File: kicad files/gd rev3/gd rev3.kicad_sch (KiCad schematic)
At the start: 0 parts

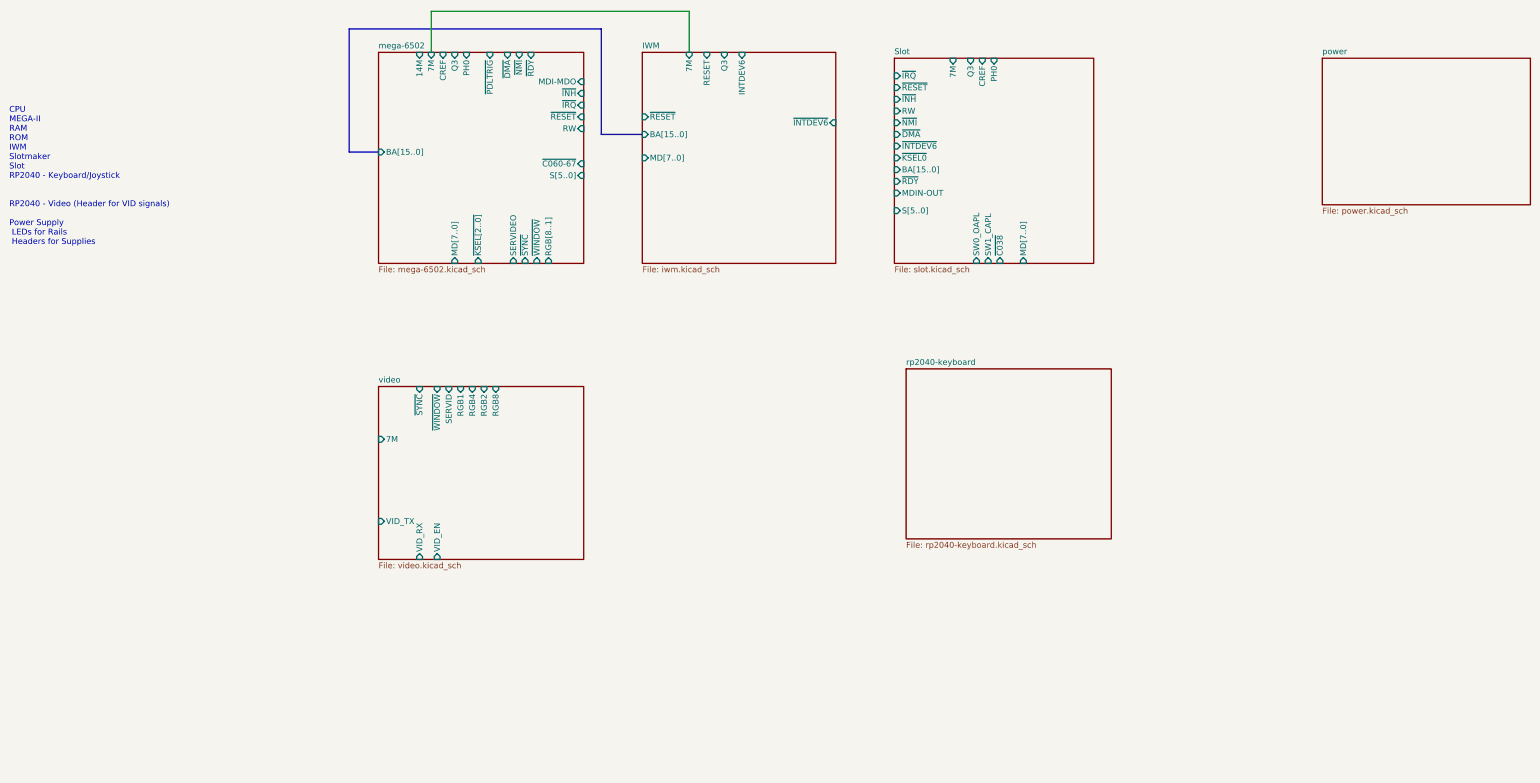
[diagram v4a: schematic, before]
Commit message: KBD Video and Power sheet labels, initial create
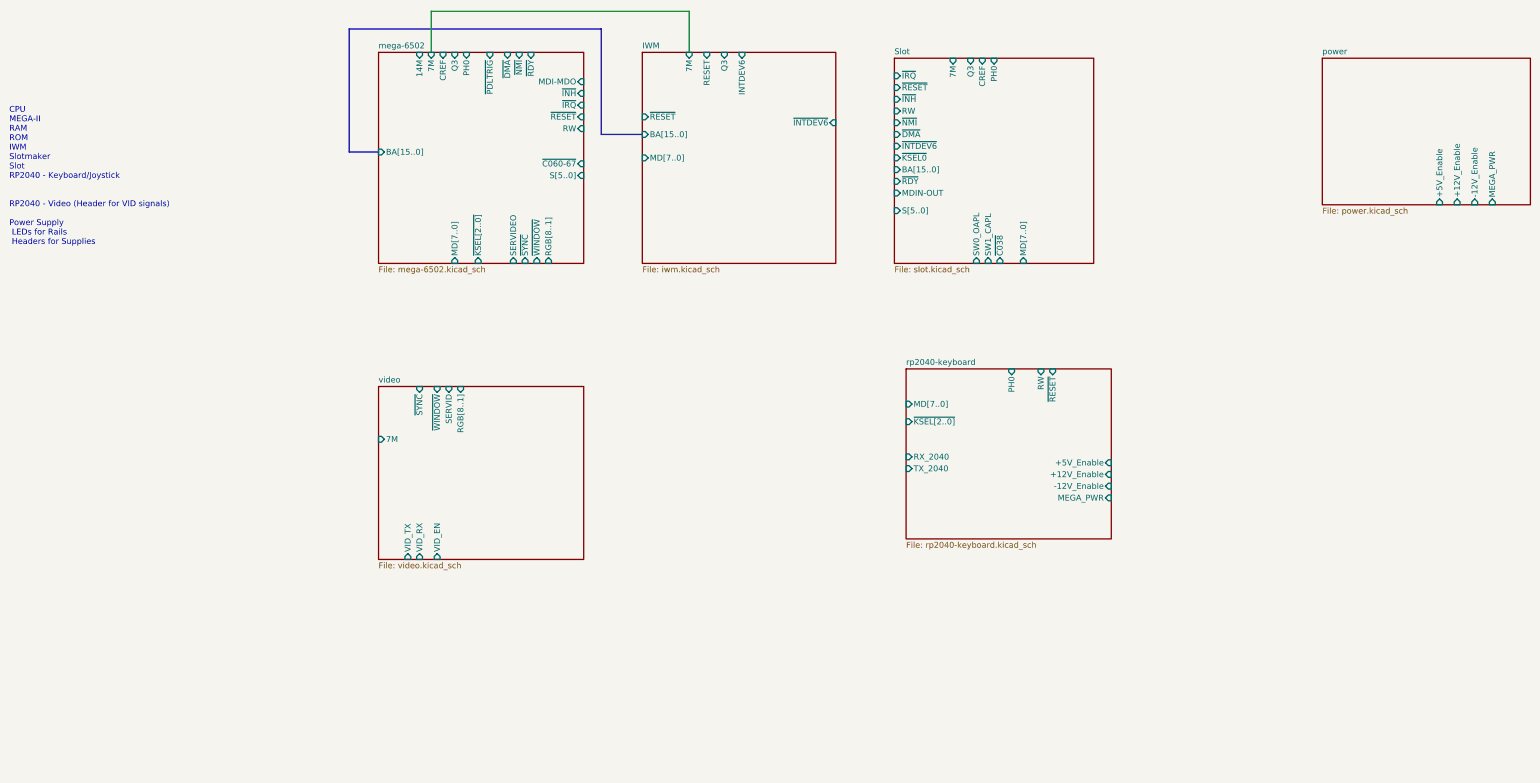
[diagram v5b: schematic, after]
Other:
- sheet power ports: added +12V_Enable, +5V_Enable, -12V_Enable, MEGA_PWR; removed none
- sheet rp2040-keyboard ports: added +12V_Enable, +5V_Enable, -12V_Enable, MD[7..0], MEGA_PWR, PH0, RW, RX_2040, TX_2040, ~{KSEL[2..0]}, ~{RESET}; removed none
- sheet video ports: added RGB[8..1]; removed RGB1, RGB2, RGB4, RGB8
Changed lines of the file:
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@@
       (effects (font (size 1.27 1.27)) (justify left))
-    )
-    (pin "RGB8" input (at 54.61 102.87 90)
-      (effects (font (size 1.27 1.27)) (justify right))
-    )
-    (pin "RGB2" input (at 52.07 102.87 90)
-      (effects (font (size 1.27 1.27)) (justify right))
-    )
-    (pin "RGB4" input (at 49.53 102.87 90)
-      (effects (font (size 1.27 1.27)) (justify right))
-    )
-    (pin "RGB1" input (at 46.99 102.87 90)
-      (effects (font (size 1.27 1.27)) (justify right))
     )
     (pin "SERVID" input (at 44.45 102.87 90)
@@
       (effects (font (size 1.27 1.27)) (justify right))
     )
-    (pin "VID_TX" input (at 29.21 132.08 180)
+    (pin "VID_TX" input (at 35.56 140.335 270)
       (effects (font (size 1.27 1.27)) (justify left))
     )
@@
     (pin "VID_EN" input (at 41.91 140.335 270)
       (effects (font (size 1.27 1.27)) (justify left))
+    )
+    (pin "RGB[8..1]" input (at 46.99 102.87 90)
+      (effects (font (size 1.27 1.27)) (justify right))
     )
   )
@@
       (effects (font (size 1.27 1.27)) (justify left top))
     )
+    (pin "+12V_Enable" input (at 262.89 63.5 270)
+      (effects (font (size 1.27 1.27)) (justify left))
+    )
+    (pin "-12V_Enable" input (at 266.7 63.5 270)
+      (effects (font (size 1.27 1.27)) (justify left))
+    )
+    (pin "MEGA_PWR" input (at 270.51 63.5 270)
+      (effects (font (size 1.27 1.27)) (justify left))
+    )
+    (pin "+5V_Enable" input (at 259.08 63.5 270)
+      (effects (font (size 1.27 1.27)) (justify left))
+    )
   )
   (sheet (at 86.36 30.48) (size 41.91 45.72) (fields_autoplaced)
@@
     (property "Sheet file" "rp2040-keyboard.kicad_sch" (id 1) (at 143.51 136.4746 0)
       (effects (font (size 1.27 1.27)) (justify left top))
+    )
+    (pin "MD[7..0]" input (at 143.51 106.68 180)
+      (effects (font (size 1.27 1.27)) (justify left))
+    )
+    (pin "PH0" input (at 166.37 99.06 90)
+      (effects (font (size 1.27 1.27)) (justify right))
+    )
+    (pin "~{RESET}" input (at 175.26 99.06 90)
+      (effects (font (size 1.27 1.27)) (justify right))
+    )
+    (pin "RW" input (at 172.72 99.06 90)
+      (effects (font (size 1.27 1.27)) (justify right))
+    )
+    (pin "~{KSEL[2..0]}" input (at 143.51 110.49 180)
+      (effects (font (size 1.27 1.27)) (justify left))
+    )
+    (pin "RX_2040" input (at 143.51 118.11 180)
+      (effects (font (size 1.27 1.27)) (justify left))
+    )
+    (pin "TX_2040" input (at 143.51 120.65 180)
+      (effects (font (size 1.27 1.27)) (justify left))
+    )
+    (pin "+5V_Enable" input (at 187.96 119.38 0)
+      (effects (font (size 1.27 1.27)) (justify right))
+    )
+    (pin "-12V_Enable" input (at 187.96 124.46 0)
+      (effects (font (size 1.27 1.27)) (justify right))
+    )
+    (pin "+12V_Enable" input (at 187.96 121.92 0)
+      (effects (font (size 1.27 1.27)) (justify right))
+    )
+    (pin "MEGA_PWR" input (at 187.96 127 0)
+      (effects (font (size 1.27 1.27)) (justify right))
     )
   )
@@
       (reference "#PWR?") (unit 1) (value "GND") (footprint "")
     )
+    (path "/adee9709-3834-4416-bb9d-b047d3f7f3b7/69eff23a-13d2-4c8a-b922-c69e1b1342c8"
+      (reference "#PWR?") (unit 1) (value "+5V") (footprint "")
+    )
     (path "/2042a325-d69f-458d-bba3-20db010e4abe/6d2d7a82-e1cb-4d5e-84e0-4b10618362c3"
       (reference "#PWR?") (unit 1) (value "+5V") (footprint "")
@@
       (reference "#PWR?") (unit 1) (value "+5V") (footprint "")
     )
+    (path "/adee9709-3834-4416-bb9d-b047d3f7f3b7/a3e1bccf-9bcb-4cf9-a57d-f7011af8db95"
+      (reference "#PWR?") (unit 1) (value "GND") (footprint "")
+    )
     (path "/2042a325-d69f-458d-bba3-20db010e4abe/c7f91c12-aad1-4af2-9146-f3ca14261f3c"
       (reference "#PWR?") (unit 1) (value "-5V") (footprint "")
@@
       (reference "C54") (unit 1) (value "1uF") (footprint "Capacitor_SMD:C_0805_2012Metric")
     )
+    (path "/adee9709-3834-4416-bb9d-b047d3f7f3b7/030ca19c-2677-4b33-9b15-9b1b03dcebad"
+      (reference "C?") (unit 1) (value "10u") (footprint "Capacitor_SMD:C_0805_2012Metric")
+    )
     (path "/2042a325-d69f-458d-bba3-20db010e4abe/2c2d225b-2075-49a0-a137-ad5a26bfee7b"
       (reference "C?") (unit 1) (value "10u") (footprint "Capacitor_SMD:C_0805_2012Metric")
@@
     )
     (path "/adee9709-3834-4416-bb9d-b047d3f7f3b7/f27ac65f-ef95-4f46-b057-5c6c2922898e"
-      (reference "SW5") (unit 1) (value "MEGA Reset") (footprint "My Libraries:SW_Push_CK_PTS525_SM15")
+      (reference "SW5") (unit 1) (value "MEGA PWR") (footprint "My Libraries:SW_Push_CK_PTS525_SM15")
     )
     (path "/6a149b4b-ed06-4835-866e-dda84632058d/0203380e-b28a-4338-964a-4e3ad6eb6d38"

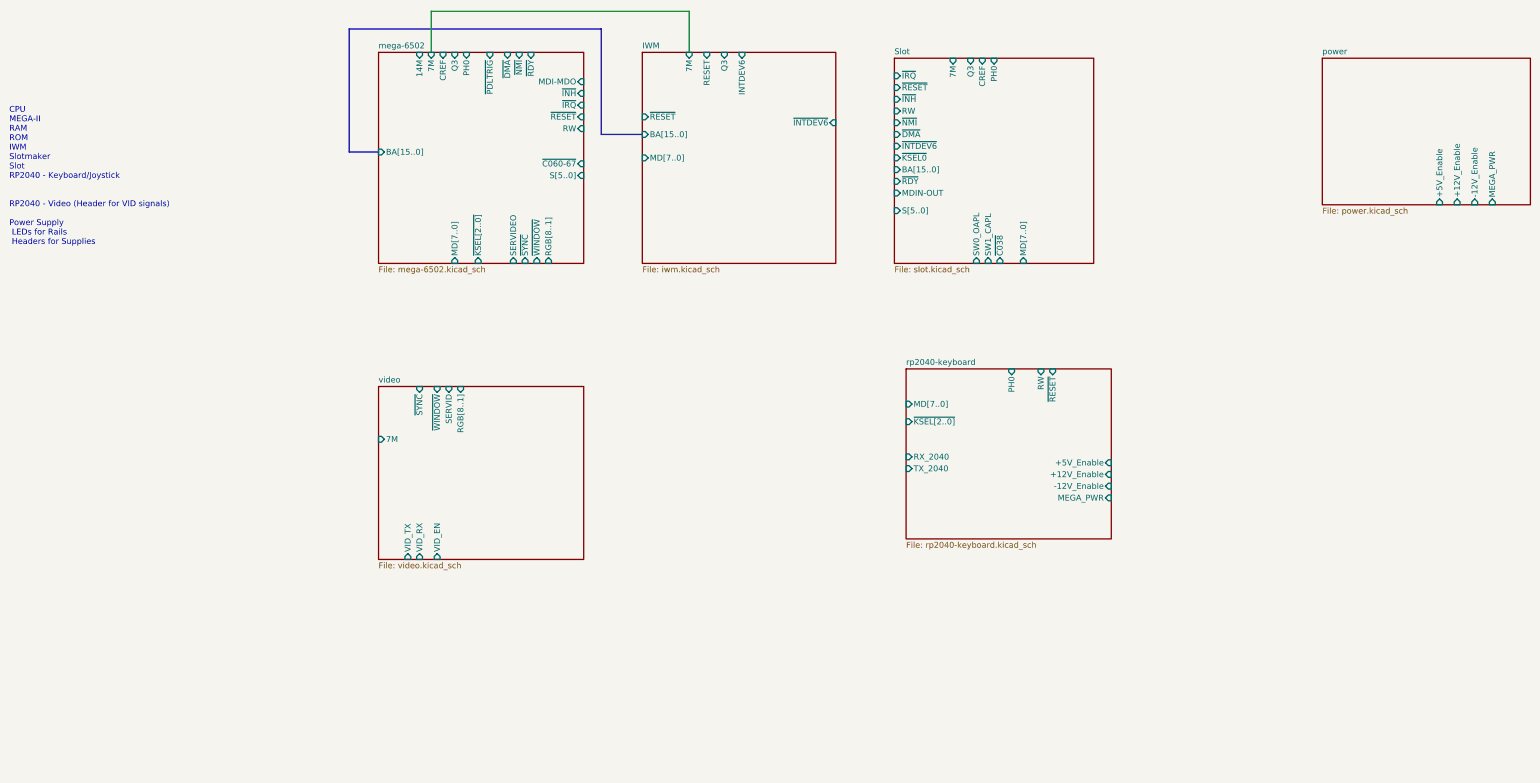
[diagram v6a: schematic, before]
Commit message: after crash commit. arranging high-level sheet signals (and added audio circuit)
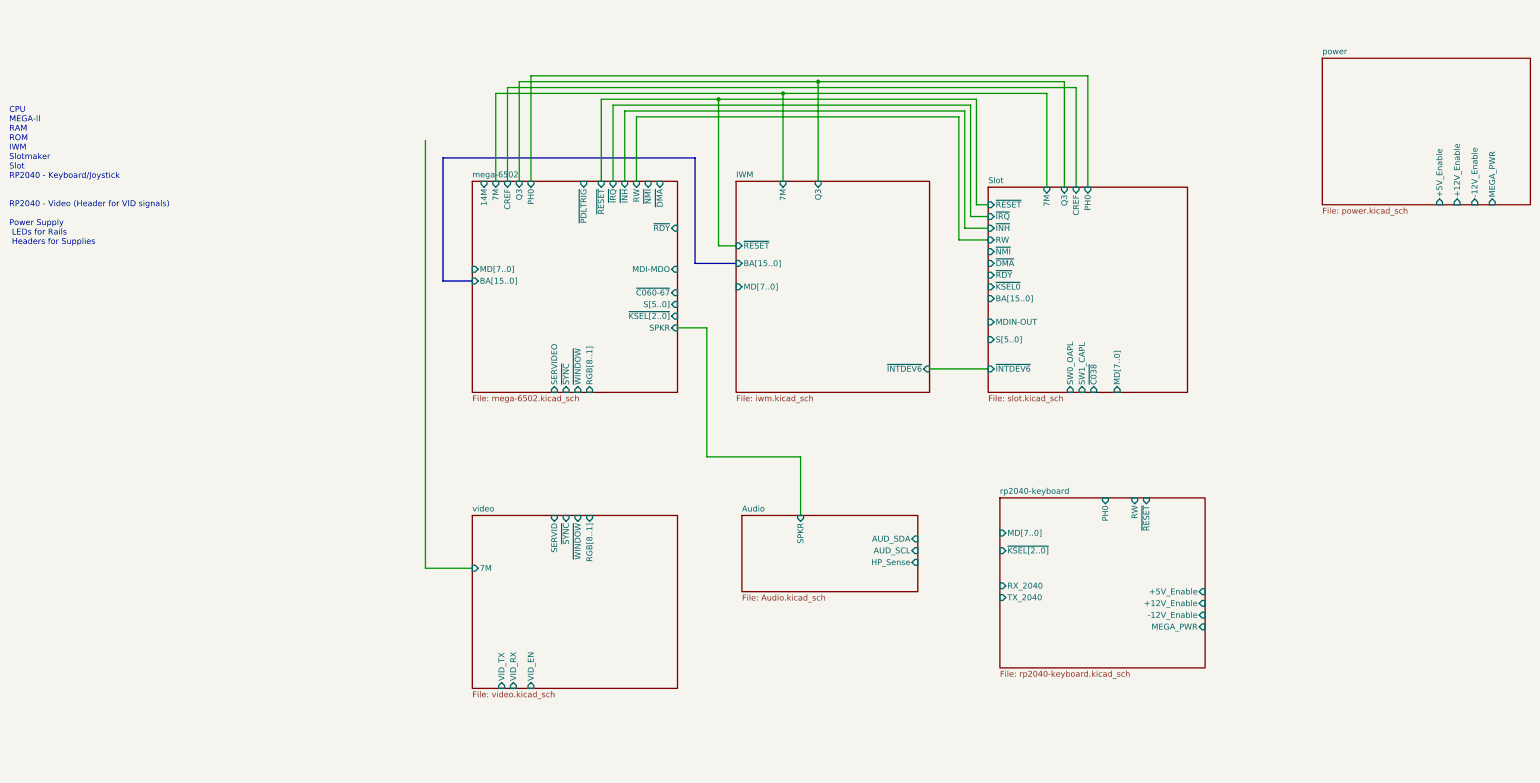
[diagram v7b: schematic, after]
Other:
- added sheet Audio (Audio.kicad_sch)
- sheet IWM ports: added none; removed INTDEV6, RESET
- sheet mega-6502 ports: added SPKR; removed none

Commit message: top-level arragements, many more works to do
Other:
- sheet mega-6502 ports: added SERVID; removed SERVIDEO
- note added: "CPU MEGA-II RAM ROM IWM Slotmaker Slot RP2040 - Keyboard/Joystick -To joystick or to USB HID Gamepad... what to do? RP2040 - Video (Header for VID signals) Power Supply LEDs for Rails Headers for Supplies"
- note removed: "CPU MEGA-II RAM ROM IWM Slotmaker Slot RP2040 - Keyboard/Joystick RP2040 - Video (Header for VID signals) Power Supply LEDs for Rails Headers for Supplies"
